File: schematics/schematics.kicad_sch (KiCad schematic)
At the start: 6 parts, among them K1 3V, Q1 Q_NPN_BCE

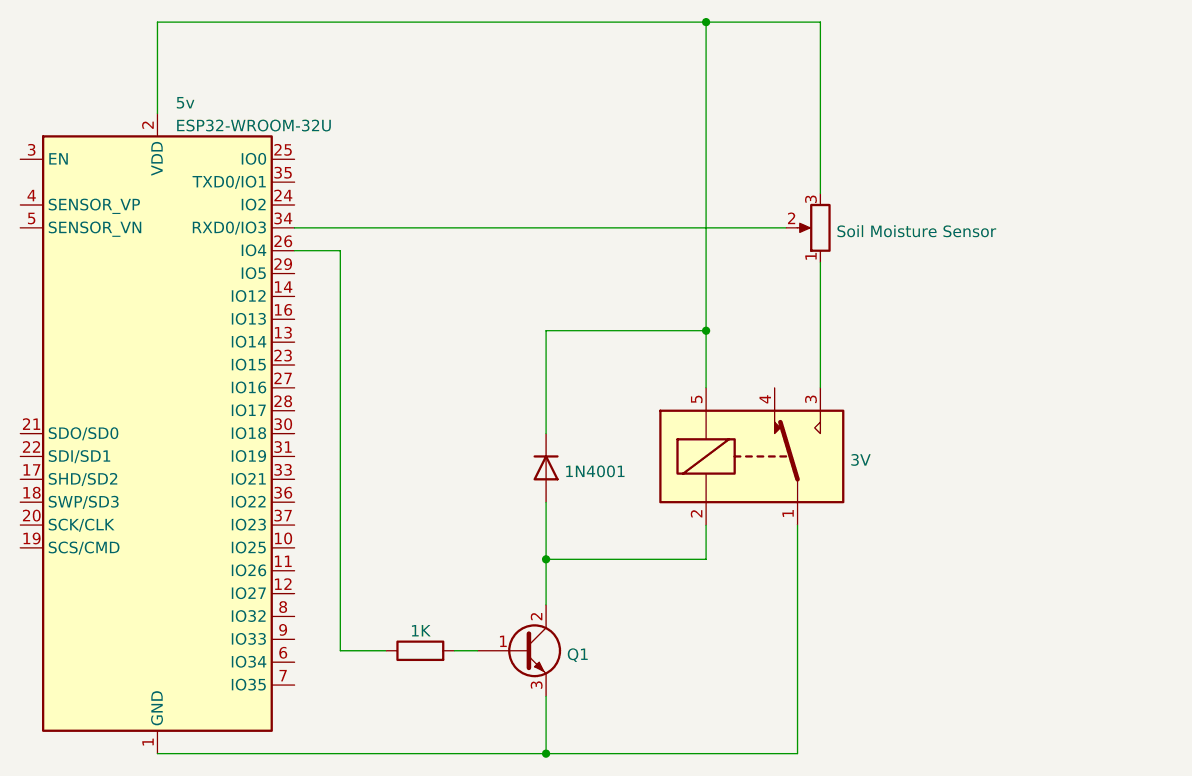
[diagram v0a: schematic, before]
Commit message: Introduce LDR sensor
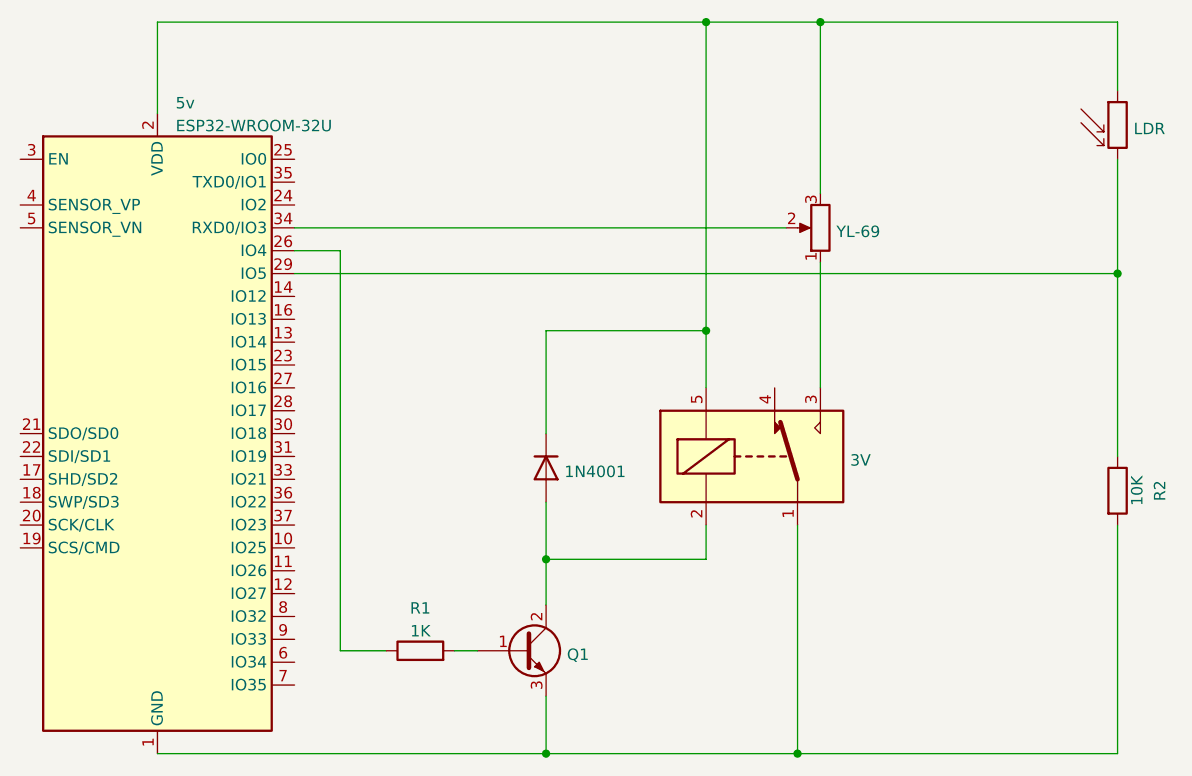
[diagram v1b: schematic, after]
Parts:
- added LDR: R_Photo, symbol Device:R_Photo
- added R2: 10K, symbol Device:R
- RV1: value Soil Moisture Sensor -> YL-69
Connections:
- net at 5v.2 (VDD), D1.1 (K), K1.5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: now also LDR.1
- net at 5v.1 (GND), 5v.15 (GND), 5v.38 (GND)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: now also R2.2
- net at 5v.29 (IO5): now also LDR.2, R2.1
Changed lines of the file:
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@@
   (junction (at 101.6 102.87) (diameter 0) (color 0 0 0 0)
   )
+  (junction (at 165.1 71.12) (diameter 0) (color 0 0 0 0)
+  )
+  (junction (at 132.08 43.18) (diameter 0) (color 0 0 0 0)
+  )
   (junction (at 119.38 43.18) (diameter 0) (color 0 0 0 0)
   )
+  (junction (at 129.54 124.46) (diameter 0) (color 0 0 0 0)
+  )
   (wire (pts (xy 101.6 102.87) (xy 101.6 107.95))
     (stroke (width 0) (type default) (color 0 0 0 0))
   )
+  (wire (pts (xy 129.54 124.46) (xy 165.1 124.46))
+    (stroke (width 0) (type default) (color 0 0 0 0))
+  )
   (wire (pts (xy 132.08 69.85) (xy 132.08 83.82))
     (stroke (width 0) (type default) (color 0 0 0 0))
@@
     (stroke (width 0) (type default) (color 0 0 0 0))
   )
+  (wire (pts (xy 165.1 71.12) (xy 165.1 91.44))
+    (stroke (width 0) (type default) (color 0 0 0 0))
+  )
+  (wire (pts (xy 165.1 58.42) (xy 165.1 71.12))
+    (stroke (width 0) (type default) (color 0 0 0 0))
+  )
   (wire (pts (xy 91.44 113.03) (xy 93.98 113.03))
     (stroke (width 0) (type default) (color 0 0 0 0))
@@
     (stroke (width 0) (type default) (color 0 0 0 0))
   )
+  (wire (pts (xy 165.1 50.8) (xy 165.1 43.18))
+    (stroke (width 0) (type default) (color 0 0 0 0))
+  )
   (wire (pts (xy 132.08 62.23) (xy 132.08 43.18))
     (stroke (width 0) (type default) (color 0 0 0 0))
@@
     (stroke (width 0) (type default) (color 0 0 0 0))
   )
+  (wire (pts (xy 165.1 43.18) (xy 132.08 43.18))
+    (stroke (width 0) (type default) (color 0 0 0 0))
+  )
+  (wire (pts (xy 73.66 71.12) (xy 165.1 71.12))
+    (stroke (width 0) (type default) (color 0 0 0 0))
+  )
   (wire (pts (xy 78.74 68.58) (xy 78.74 113.03))
     (stroke (width 0) (type default) (color 0 0 0 0))
   )
+  (wire (pts (xy 165.1 124.46) (xy 165.1 99.06))
+    (stroke (width 0) (type default) (color 0 0 0 0))
+  )
   (wire (pts (xy 101.6 118.11) (xy 101.6 124.46))
     (stroke (width 0) (type default) (color 0 0 0 0))
@@
   (wire (pts (xy 101.6 77.47) (xy 119.38 77.47))
     (stroke (width 0) (type default) (color 0 0 0 0))
+  )
+  (symbol (lib_id "Device:R_Photo") (at 165.1 54.61 0) (unit 1)
+    (in_bom yes) (on_board yes) (fields_autoplaced)
+    (property "Reference" "LDR" (id 0) (at 166.878 55.0438 0)
+      (effects (font (size 1.27 1.27)) (justify left))
+    )
+    (property "Value" "R_Photo" (id 1) (at 166.878 56.3122 0)
+      (effects (font (size 1.27 1.27)) (justify left) hide)
+    )
+    (property "Footprint" "" (id 2) (at 166.37 60.96 90)
+      (effects (font (size 1.27 1.27)) (justify left) hide)
+    )
+    (property "Datasheet" "~" (id 3) (at 165.1 55.88 0)
+      (effects (font (size 1.27 1.27)) hide)
+    )
+    (pin "1")
+    (pin "2")
   )
   (symbol (lib_id "Diode:1N4001") (at 101.6 92.71 270) (unit 1)
@@
   (symbol (lib_id "Device:R") (at 87.63 113.03 90) (unit 1)
     (in_bom yes) (on_board yes)
-    (property "Reference" "R1" (id 0) (at 87.63 108.3142 90)
-      (effects (font (size 1.27 1.27)) hide)
-    )
+    (property "Reference" "R1" (id 0) (at 87.63 108.3142 90))
     (property "Value" "1K" (id 1) (at 87.63 110.8512 90))
     (property "Footprint" "" (id 2) (at 87.63 114.808 90)
@@
     (pin "2")
   )
+  (symbol (lib_id "Device:R") (at 165.1 95.25 0) (unit 1)
+    (in_bom yes) (on_board yes)
+    (property "Reference" "R2" (id 0) (at 169.8158 95.25 90))
+    (property "Value" "10K" (id 1) (at 167.2788 95.25 90))
+    (property "Footprint" "" (id 2) (at 163.322 95.25 90)
+      (effects (font (size 1.27 1.27)) hide)
+    )
+    (property "Datasheet" "~" (id 3) (at 165.1 95.25 0)
+      (effects (font (size 1.27 1.27)) hide)
+    )
+    (pin "1")
+    (pin "2")
+  )
   (symbol (lib_id "Device:R_Potentiometer") (at 132.08 66.04 180) (unit 1)
     (in_bom yes) (on_board yes) (fields_autoplaced)
@@
       (effects (font (size 1.27 1.27)) (justify right) hide)
     )
-    (property "Value" "Soil Moisture Sensor" (id 1) (at 133.858 66.4738 0)
+    (property "Value" "YL-69" (id 1) (at 133.858 66.4738 0)
       (effects (font (size 1.27 1.27)) (justify right))
     )
@@
       (reference "K1") (unit 1) (value "3V") (footprint "Relay_THT:Relay_SPDT_SANYOU_SRD_Series_Form_C")
     )
+    (path "/0f8f7f8e-7c24-43c8-b7b5-d169604531e5"
+      (reference "LDR") (unit 1) (value "R_Photo") (footprint "")
+    )
     (path "/8623b812-4f38-45fc-86bf-8aca6c587a6e"
       (reference "Q1") (unit 1) (value "Q_NPN_BCE") (footprint "")
@@
       (reference "R1") (unit 1) (value "1K") (footprint "")
     )
+    (path "/9b1bb4e7-b2fc-4629-8b8c-50c6ee7e1604"
+      (reference "R2") (unit 1) (value "10K") (footprint "")
+    )
     (path "/a0c29daa-7e45-4f91-a2b3-1aeb42edf886"
-      (reference "RV1") (unit 1) (value "Soil Moisture Sensor") (footprint "")
-    )
-  )
+      (reference "RV1") (unit 1) (value "YL-69") (footprint "")
+    )
+  )
